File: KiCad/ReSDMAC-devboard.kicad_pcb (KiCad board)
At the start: 4 copper layers, 101.6 x 47 mm, 7 parts, among them J2 USB_B_Micro, J3 Conn_02x01, U1 PLCC-84-Plug, U2 Super_DMAC_SMD_socket, U3 Super_DMAC_TH_socket

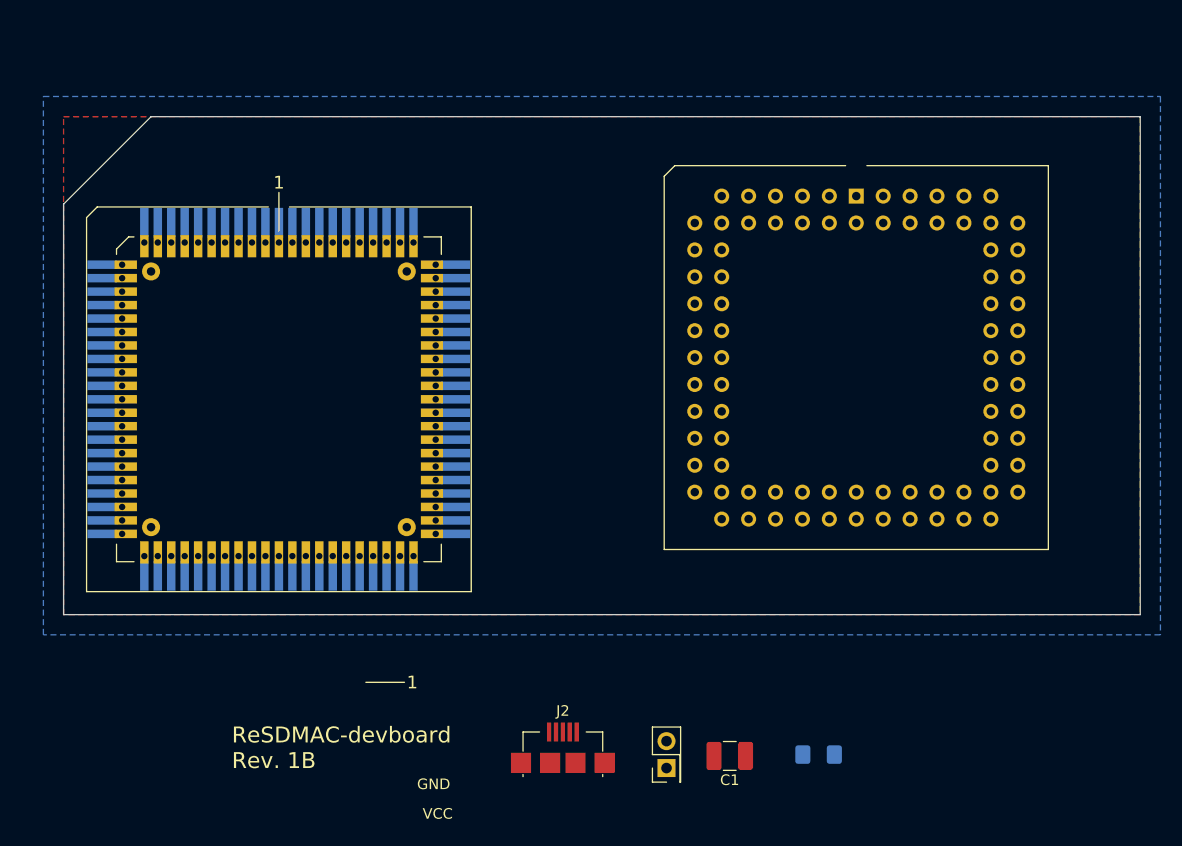
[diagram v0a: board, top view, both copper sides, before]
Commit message: Added nets and started routing
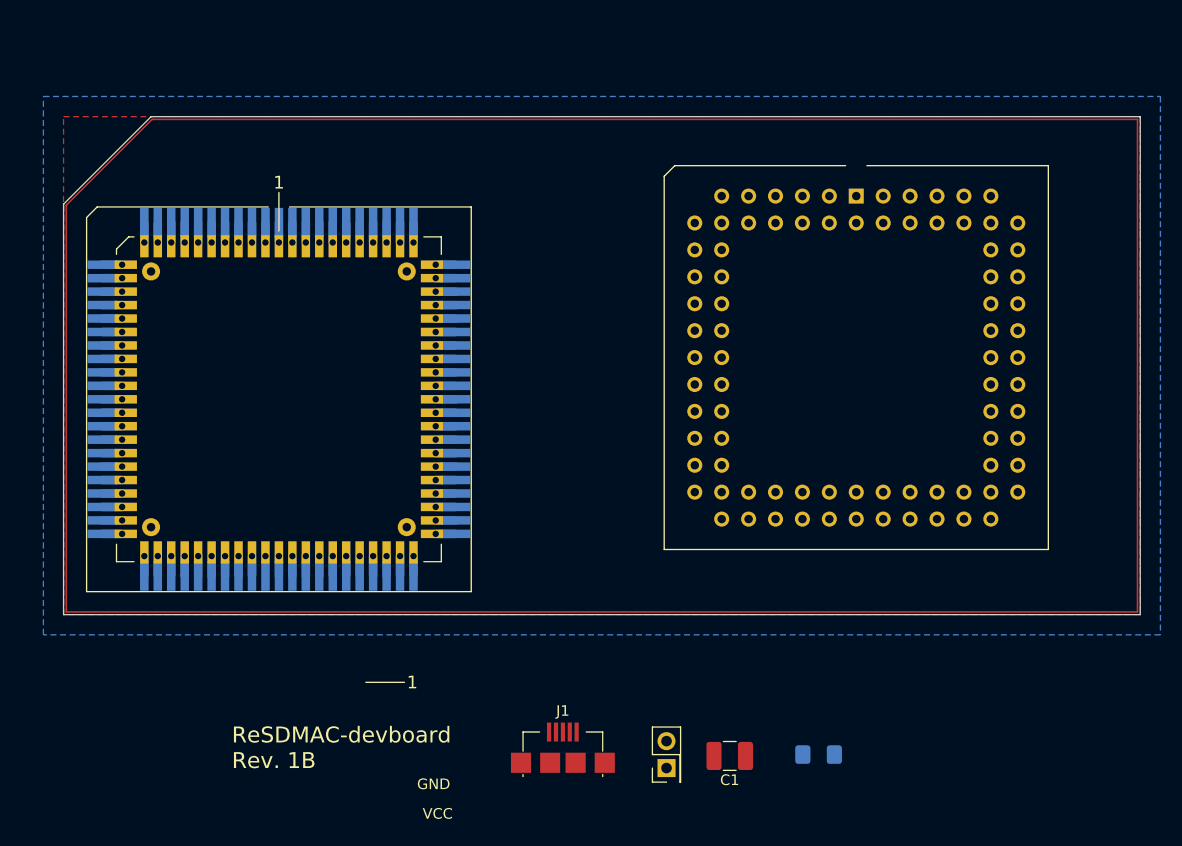
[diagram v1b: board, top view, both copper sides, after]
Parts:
- renumbered J2 to J1, J3 to J2
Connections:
- J1 pad 1: /VIN -> VCC
- J2 pad 1: /VIN -> VCC
- U1 pad 1: Net-(U1-Pad1) -> D0
- U1 pad 10: Net-(U1-Pad10) -> D9
- U1 pad 11: Net-(U1-Pad11) -> D10
- U1 pad 12: Net-(U1-Pad12) -> D11
- U1 pad 13: Net-(U1-Pad13) -> D12
- U1 pad 14: Net-(U1-Pad14) -> D13
- U1 pad 15: Net-(U1-Pad15) -> D14
- U1 pad 16: Net-(U1-Pad16) -> D15
- U1 pad 17: Net-(U1-Pad17) -> D16
- U1 pad 18: Net-(U1-Pad18) -> D17
- U1 pad 19: Net-(U1-Pad19) -> D18
- U1 pad 2: Net-(U1-Pad2) -> D1
- U1 pad 20: Net-(U1-Pad20) -> D19
- U1 pad 22: Net-(U1-Pad22) -> D20
- U1 pad 23: Net-(U1-Pad23) -> D21
- U1 pad 24: Net-(U1-Pad24) -> D22
- U1 pad 25: Net-(U1-Pad25) -> D23
- U1 pad 26: Net-(U1-Pad26) -> D24
- U1 pad 27: Net-(U1-Pad27) -> D25
- U1 pad 28: Net-(U1-Pad28) -> D26
- U1 pad 29: Net-(U1-Pad29) -> D27
- U1 pad 3: Net-(U1-Pad3) -> D2
- U1 pad 30: Net-(U1-Pad30) -> D28
- U1 pad 31: Net-(U1-Pad31) -> D29
- U1 pad 32: Net-(U1-Pad32) -> D30
- U1 pad 33: Net-(U1-Pad33) -> D31
- U1 pad 34: Net-(U1-Pad34) -> INTB
- U1 pad 35: Net-(U1-Pad35) -> INT2
- U1 pad 36: Net-(U1-Pad36) -> SIZ1
- U1 pad 37: Net-(U1-Pad37) -> RW
- U1 pad 38: Net-(U1-Pad38) -> AS
- U1 pad 39: Net-(U1-Pad39) -> DS
- U1 pad 4: Net-(U1-Pad4) -> D3
- U1 pad 40: Net-(U1-Pad40) -> DSACK1
- U1 pad 41: Net-(U1-Pad41) -> DSACK0
- U1 pad 43: Net-(U1-Pad43) -> STERM
- U1 pad 44: Net-(U1-Pad44) -> CPUCLK
- U1 pad 45: Net-(U1-Pad45) -> SCSI
- U1 pad 46: Net-(U1-Pad46) -> IORST
- U1 pad 47: Net-(U1-Pad47) -> BERR
- U1 pad 48: Net-(U1-Pad48) -> PD0
- U1 pad 49: Net-(U1-Pad49) -> PD1
- U1 pad 5: Net-(U1-Pad5) -> D4
- U1 pad 50: Net-(U1-Pad50) -> PD2
- U1 pad 51: Net-(U1-Pad51) -> PD3
- U1 pad 52: Net-(U1-Pad52) -> PD4
- U1 pad 53: Net-(U1-Pad53) -> PD5
- U1 pad 54: Net-(U1-Pad54) -> PD6
- U1 pad 55: Net-(U1-Pad55) -> PD7
- U1 pad 56: Net-(U1-Pad56) -> PD8
- U1 pad 57: Net-(U1-Pad57) -> PD9
- U1 pad 58: Net-(U1-Pad58) -> PD10
- U1 pad 59: Net-(U1-Pad59) -> PD11
- U1 pad 6: Net-(U1-Pad6) -> D5
- U1 pad 60: Net-(U1-Pad60) -> PD12
- U1 pad 62: Net-(U1-Pad62) -> PD14
- U1 pad 64: Net-(U1-Pad64) -> PD15
- U1 pad 65: Net-(U1-Pad65) -> DREQ
- U1 pad 66: Net-(U1-Pad66) -> DACK
- U1 pad 67: Net-(U1-Pad67) -> CSS
- U1 pad 68: Net-(U1-Pad68) -> IOW
- U1 pad 69: Net-(U1-Pad69) -> IOR
- U1 pad 7: Net-(U1-Pad7) -> D6
- U1 pad 70: Net-(U1-Pad70) -> CSX0
- U1 pad 71: Net-(U1-Pad71) -> CSX1
- U1 pad 72: Net-(U1-Pad72) -> IORDY
- U1 pad 73: Net-(U1-Pad73) -> INTA
- U1 pad 74: Net-(U1-Pad74) -> INC_ADD
- U1 pad 75: Net-(U1-Pad75) -> DMAEN
- U1 pad 76: Net-(U1-Pad76) -> A2
- U1 pad 77: Net-(U1-Pad77) -> A3
- U1 pad 78: Net-(U1-Pad78) -> A4
- U1 pad 79: Net-(U1-Pad79) -> A5
- U1 pad 8: Net-(U1-Pad8) -> D7
- U1 pad 80: Net-(U1-Pad80) -> A6
- U1 pad 81: Net-(U1-Pad81) -> SBR
- U1 pad 82: Net-(U1-Pad82) -> SBG
- U1 pad 83: Net-(U1-Pad83) -> BGACK
- U1 pad 9: Net-(U1-Pad9) -> D8
- U2 pad 1: Net-(U2-Pad1) -> D0
- U2 pad 10: Net-(U2-Pad10) -> D9
- U2 pad 11: Net-(U2-Pad11) -> D10
- U2 pad 12: Net-(U2-Pad12) -> D11
- U2 pad 13: Net-(U2-Pad13) -> D12
- U2 pad 14: Net-(U2-Pad14) -> D13
- U2 pad 15: Net-(U2-Pad15) -> D14
- U2 pad 16: Net-(U2-Pad16) -> D15
- U2 pad 17: Net-(U2-Pad17) -> D16
- U2 pad 18: Net-(U2-Pad18) -> D17
- U2 pad 19: Net-(U2-Pad19) -> D18
- U2 pad 2: Net-(U2-Pad2) -> D1
- U2 pad 20: Net-(U2-Pad20) -> D19
- U2 pad 22: Net-(U2-Pad22) -> D20
- U2 pad 23: Net-(U2-Pad23) -> D21
- U2 pad 24: Net-(U2-Pad24) -> D22
- U2 pad 25: Net-(U2-Pad25) -> D23
- U2 pad 26: Net-(U2-Pad26) -> D24
- U2 pad 27: Net-(U2-Pad27) -> D25
- U2 pad 28: Net-(U2-Pad28) -> D26
- U2 pad 29: Net-(U2-Pad29) -> D27
- U2 pad 3: Net-(U2-Pad3) -> D2
- U2 pad 30: Net-(U2-Pad30) -> D28
- U2 pad 31: Net-(U2-Pad31) -> D29
- U2 pad 32: Net-(U2-Pad32) -> D30
- U2 pad 33: Net-(U2-Pad33) -> D31
- U2 pad 34: Net-(U2-Pad34) -> INTB
- U2 pad 35: Net-(U2-Pad35) -> INT2
- U2 pad 36: Net-(U2-Pad36) -> SIZ1
- U2 pad 37: Net-(U2-Pad37) -> RW
- U2 pad 38: Net-(U2-Pad38) -> AS
- U2 pad 39: Net-(U2-Pad39) -> DS
- U2 pad 4: Net-(U2-Pad4) -> D3
- U2 pad 40: Net-(U2-Pad40) -> DSACK1
- U2 pad 41: Net-(U2-Pad41) -> DSACK0
- U2 pad 43: Net-(U2-Pad43) -> STERM
- U2 pad 44: Net-(U2-Pad44) -> CPUCLK
- U2 pad 45: Net-(U2-Pad45) -> SCSI
- U2 pad 46: Net-(U2-Pad46) -> IORST
- U2 pad 47: Net-(U2-Pad47) -> BERR
- U2 pad 48: Net-(U2-Pad48) -> PD0
- U2 pad 49: Net-(U2-Pad49) -> PD1
- U2 pad 5: Net-(U2-Pad5) -> D4
- U2 pad 50: Net-(U2-Pad50) -> PD2
- U2 pad 51: Net-(U2-Pad51) -> PD3
- U2 pad 52: Net-(U2-Pad52) -> PD4
- U2 pad 53: Net-(U2-Pad53) -> PD5
- U2 pad 54: Net-(U2-Pad54) -> PD6
- U2 pad 55: Net-(U2-Pad55) -> PD7
- U2 pad 56: Net-(U2-Pad56) -> PD8
- U2 pad 57: Net-(U2-Pad57) -> PD9
- U2 pad 58: Net-(U2-Pad58) -> PD10
- U2 pad 59: Net-(U2-Pad59) -> PD11
- U2 pad 6: Net-(U2-Pad6) -> D5
- U2 pad 60: Net-(U2-Pad60) -> PD12
- U2 pad 62: Net-(U2-Pad62) -> PD14
- U2 pad 64: Net-(U2-Pad64) -> PD15
- U2 pad 65: Net-(U2-Pad65) -> DREQ
- U2 pad 66: Net-(U2-Pad66) -> DACK
- U2 pad 67: Net-(U2-Pad67) -> CSS
- U2 pad 68: Net-(U2-Pad68) -> IOW
- U2 pad 69: Net-(U2-Pad69) -> IOR
- U2 pad 7: Net-(U2-Pad7) -> D6
- U2 pad 70: Net-(U2-Pad70) -> CSX0
- U2 pad 71: Net-(U2-Pad71) -> CSX1
- U2 pad 72: Net-(U2-Pad72) -> IORDY
- U2 pad 73: Net-(U2-Pad73) -> INTA
- U2 pad 74: Net-(U2-Pad74) -> INC_ADD
- U2 pad 75: Net-(U2-Pad75) -> DMAEN
- U2 pad 76: Net-(U2-Pad76) -> A2
- U2 pad 77: Net-(U2-Pad77) -> A3
- U2 pad 78: Net-(U2-Pad78) -> A4
- U2 pad 79: Net-(U2-Pad79) -> A5
- U2 pad 8: Net-(U2-Pad8) -> D7
- U2 pad 80: Net-(U2-Pad80) -> A6
- U2 pad 81: Net-(U2-Pad81) -> SBR
- U2 pad 82: Net-(U2-Pad82) -> SBG
- U2 pad 83: Net-(U2-Pad83) -> BGACK
- U2 pad 9: Net-(U2-Pad9) -> D8
- U3 pad 1: Net-(U3-Pad1) -> D0
- U3 pad 10: Net-(U3-Pad10) -> D9
- U3 pad 11: Net-(U3-Pad11) -> D10
- U3 pad 12: Net-(U3-Pad12) -> D11
- U3 pad 13: Net-(U3-Pad13) -> D12
- U3 pad 14: Net-(U3-Pad14) -> D13
- U3 pad 15: Net-(U3-Pad15) -> D14
- U3 pad 16: Net-(U3-Pad16) -> D15
- U3 pad 17: Net-(U3-Pad17) -> D16
- U3 pad 18: Net-(U3-Pad18) -> D17
- U3 pad 19: Net-(U3-Pad19) -> D18
- U3 pad 2: Net-(U3-Pad2) -> D1
- U3 pad 20: Net-(U3-Pad20) -> D19
- U3 pad 22: Net-(U3-Pad22) -> D20
- U3 pad 23: Net-(U3-Pad23) -> D21
- U3 pad 24: Net-(U3-Pad24) -> D22
- U3 pad 25: Net-(U3-Pad25) -> D23
- U3 pad 26: Net-(U3-Pad26) -> D24
- U3 pad 27: Net-(U3-Pad27) -> D25
- U3 pad 28: Net-(U3-Pad28) -> D26
- U3 pad 29: Net-(U3-Pad29) -> D27
- U3 pad 3: Net-(U3-Pad3) -> D2
- U3 pad 30: Net-(U3-Pad30) -> D28
- U3 pad 31: Net-(U3-Pad31) -> D29
- U3 pad 32: Net-(U3-Pad32) -> D30
- U3 pad 33: Net-(U3-Pad33) -> D31
- U3 pad 34: Net-(U3-Pad34) -> INTB
- U3 pad 35: Net-(U3-Pad35) -> INT2
- U3 pad 36: Net-(U3-Pad36) -> SIZ1
- U3 pad 37: Net-(U3-Pad37) -> RW
- U3 pad 38: Net-(U3-Pad38) -> AS
- U3 pad 39: Net-(U3-Pad39) -> DS
- U3 pad 4: Net-(U3-Pad4) -> D3
- U3 pad 40: Net-(U3-Pad40) -> DSACK1
- U3 pad 41: Net-(U3-Pad41) -> DSACK0
- U3 pad 43: Net-(U3-Pad43) -> STERM
- U3 pad 44: Net-(U3-Pad44) -> CPUCLK
- U3 pad 45: Net-(U3-Pad45) -> SCSI
- U3 pad 46: Net-(U3-Pad46) -> IORST
- U3 pad 47: Net-(U3-Pad47) -> BERR
- U3 pad 48: Net-(U3-Pad48) -> PD0
- U3 pad 49: Net-(U3-Pad49) -> PD1
- U3 pad 5: Net-(U3-Pad5) -> D4
- U3 pad 50: Net-(U3-Pad50) -> PD2
- U3 pad 51: Net-(U3-Pad51) -> PD3
- U3 pad 52: Net-(U3-Pad52) -> PD4
- U3 pad 53: Net-(U3-Pad53) -> PD5
- U3 pad 54: Net-(U3-Pad54) -> PD6
- U3 pad 55: Net-(U3-Pad55) -> PD7
- U3 pad 56: Net-(U3-Pad56) -> PD8
- U3 pad 57: Net-(U3-Pad57) -> PD9
- U3 pad 58: Net-(U3-Pad58) -> PD10
- U3 pad 59: Net-(U3-Pad59) -> PD11
- U3 pad 6: Net-(U3-Pad6) -> D5
- U3 pad 60: Net-(U3-Pad60) -> PD12
- U3 pad 62: Net-(U3-Pad62) -> PD14
- U3 pad 64: Net-(U3-Pad64) -> PD15
- U3 pad 65: Net-(U3-Pad65) -> DREQ
- U3 pad 66: Net-(U3-Pad66) -> DACK
- U3 pad 67: Net-(U3-Pad67) -> CSS
- U3 pad 68: Net-(U3-Pad68) -> IOW
- U3 pad 69: Net-(U3-Pad69) -> IOR
- U3 pad 7: Net-(U3-Pad7) -> D6
- U3 pad 70: Net-(U3-Pad70) -> CSX0
- U3 pad 71: Net-(U3-Pad71) -> CSX1
- U3 pad 72: Net-(U3-Pad72) -> IORDY
- U3 pad 73: Net-(U3-Pad73) -> INTA
- U3 pad 74: Net-(U3-Pad74) -> INC_ADD
- U3 pad 75: Net-(U3-Pad75) -> DMAEN
- U3 pad 76: Net-(U3-Pad76) -> A2
- U3 pad 77: Net-(U3-Pad77) -> A3
- U3 pad 78: Net-(U3-Pad78) -> A4
- U3 pad 79: Net-(U3-Pad79) -> A5
- U3 pad 8: Net-(U3-Pad8) -> D7
- U3 pad 80: Net-(U3-Pad80) -> A6
- U3 pad 81: Net-(U3-Pad81) -> SBR
- U3 pad 82: Net-(U3-Pad82) -> SBG
- U3 pad 83: Net-(U3-Pad83) -> BGACK
- U3 pad 9: Net-(U3-Pad9) -> D8
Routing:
- net GND: track 0.00 -> 292.3 mm
- net VCC: track 0.00 -> 3.73 mm
- net SIZ1: track 0.00 -> 1.87 mm
- net SBR: track 0.00 -> 1.87 mm
- net SBG: track 0.00 -> 1.87 mm
- net DMAEN: track 0.00 -> 1.87 mm
- net D9: track 0.00 -> 1.87 mm
- net D8: track 0.00 -> 1.87 mm
- net D7: track 0.00 -> 1.87 mm
- net D6: track 0.00 -> 1.87 mm
- net D5: track 0.00 -> 1.87 mm
- net D4: track 0.00 -> 1.87 mm
- net D30: track 0.00 -> 1.87 mm
- net D3: track 0.00 -> 1.87 mm
- net D29: track 0.00 -> 1.87 mm
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
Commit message: Routing of all traces done
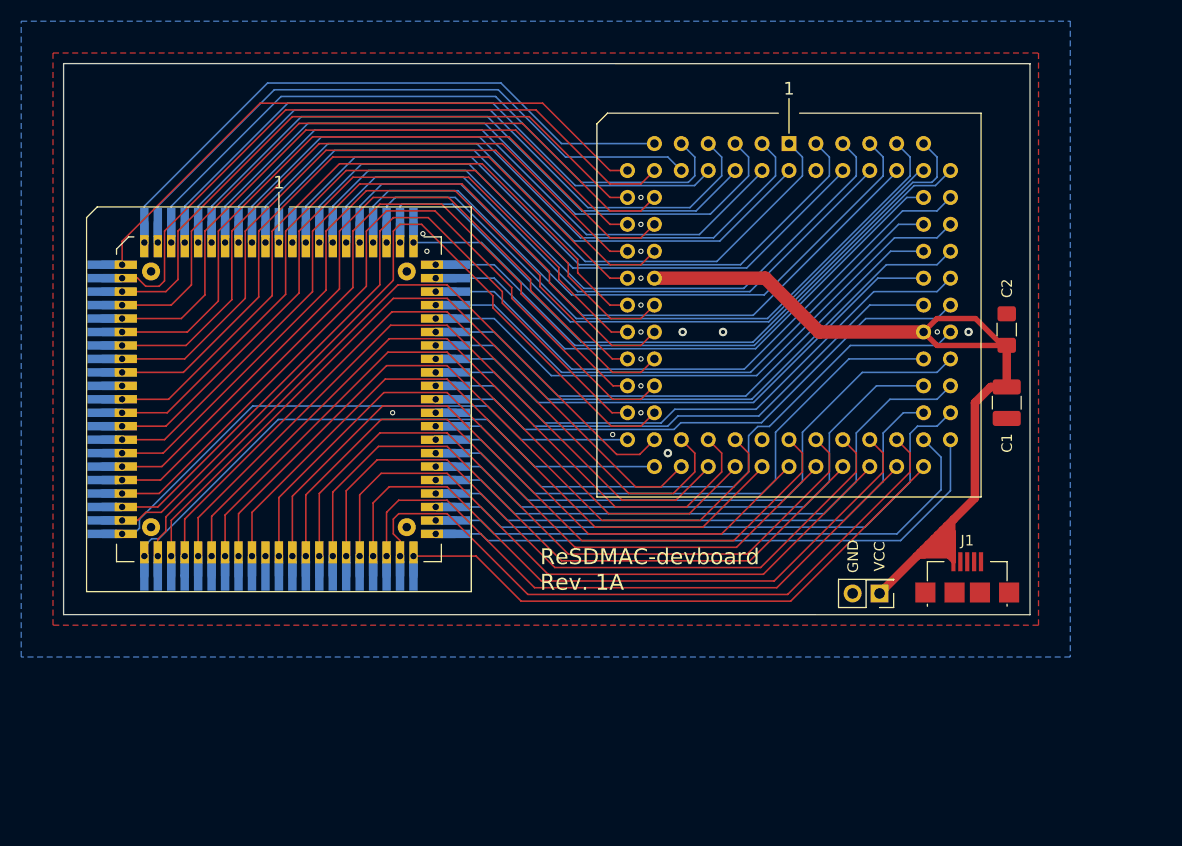
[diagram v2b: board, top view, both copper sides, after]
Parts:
- C2: moved to F.Cu
- moved C2 43.9 mm to (206.3, 109.7), turned to 270 degrees
- moved C1 42.4 mm to (206.3, 116.6), turned to 90 degrees
- moved J1 41.4 mm to (202.6, 132.2)
- moved J2 26.0 mm to (194.3, 134.6), turned to 180 degrees
- moved U3 8.05 mm to (185.8, 92.2)
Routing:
- net GND: track 292.3 -> 1.87 mm, vias 0 -> 18
- net VCC: track 3.73 -> 112.5 mm
- net D29: track 1.87 -> 75.5 mm
- net D27: track 1.87 -> 74.7 mm
- net D25: track 1.87 -> 73.8 mm
- net SIZ1: track 1.87 -> 73.1 mm
- net D23: track 1.87 -> 72.9 mm
- net AS: track 1.87 -> 72.2 mm
- net D28: track 1.87 -> 72.1 mm
- net D21: track 1.87 -> 72.1 mm
- net DSACK1: track 1.87 -> 71.3 mm
- net D26: track 1.87 -> 71.1 mm
- net CPUCLK: track 1.87 -> 70.7 mm
- net D24: track 1.87 -> 70.3 mm
- net INT2: track 1.87 -> 70.2 mm
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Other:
- board size 101.6 x 47 mm -> 91.2 x 52 mm
- board text added: "ReSDMAC-devboard Rev. 1A"
- board text removed: "ReSDMAC-devboard Rev. 1B"

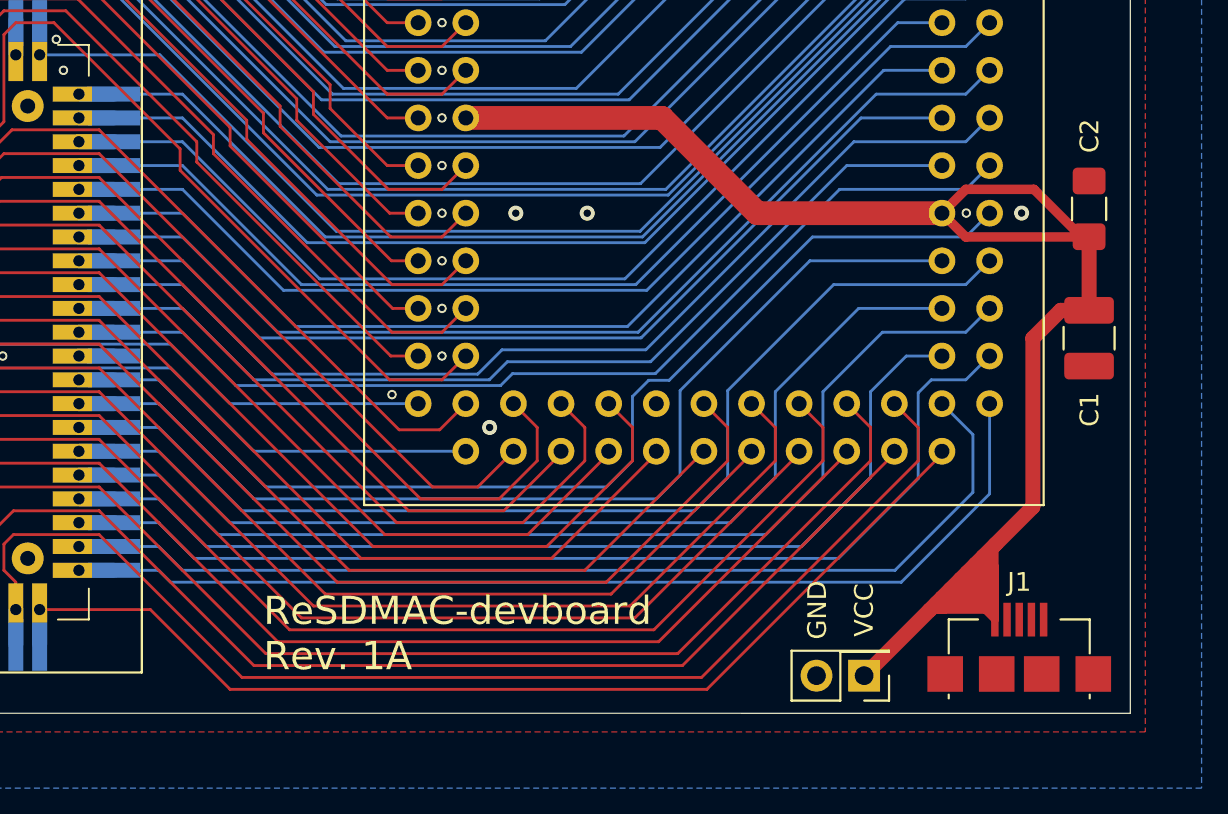
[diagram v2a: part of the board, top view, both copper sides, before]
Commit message: Fixed caps and power circuit routing
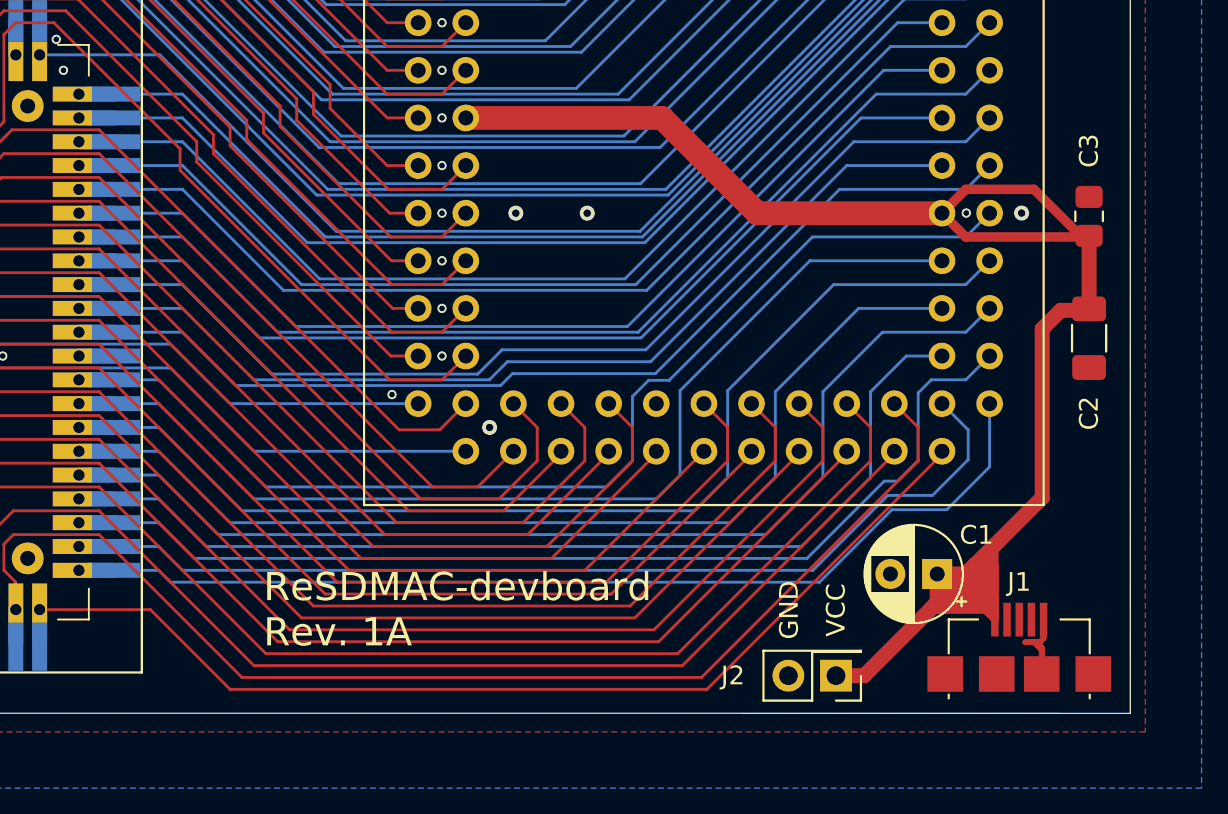
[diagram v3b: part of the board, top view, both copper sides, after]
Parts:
- added C3: 0.1uF, Capacitor_SMD:C_0805_2012Metric_Pad1.18x1.45mm_HandSolder, F.Cu at (206.3, 110.1)
- C1: value C -> 100uF Radial Pitch_2.5mm; footprint Capacitor_SMD:C_1210_3225Metric_Pad1.42x2.65mm_HandSolder -> Capacitor_THT:CP_Radial_D5.0mm_P2.50mm
- C2: value C_Small -> 10uF; footprint Capacitor_SMD:C_1206_3216Metric_Pad1.42x1.75mm_HandSolder -> Capacitor_SMD:C_1206_3216Metric_Pad1.33x1.80mm_HandSolder
- moved C1 15.0 mm to (198.2, 129.2), turned to 180 degrees
- moved C2 6.90 mm to (206.3, 116.6), turned to 90 degrees
- moved J2 1.50 mm to (192.8, 134.6)
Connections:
- C1 pad 1: GND -> VCC
- C1 pad 2: VCC -> GND
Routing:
- net GND: track 1.87 -> 8.38 mm
- net VCC: track 112.5 -> 118.4 mm
- net PD7: track 55.4 -> 54.0 mm
- net PD6: track 55.6 -> 54.8 mm
- net PD8: track 56.5 -> 56.0 mm

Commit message: Added MountingHole_3.2mm_M3_Pad_Via for grounding wire with ring lug connector
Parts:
- added J3: Conn_01x01, MountingHole:MountingHole_3.2mm_M3_Pad_Via, F.Cu at (123.3, 90.6)
